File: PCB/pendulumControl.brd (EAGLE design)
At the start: 48 x 41.1 mm, 31 parts, among them IC1 PIC32MX340F512H, IC2 LT1963EST-3.3

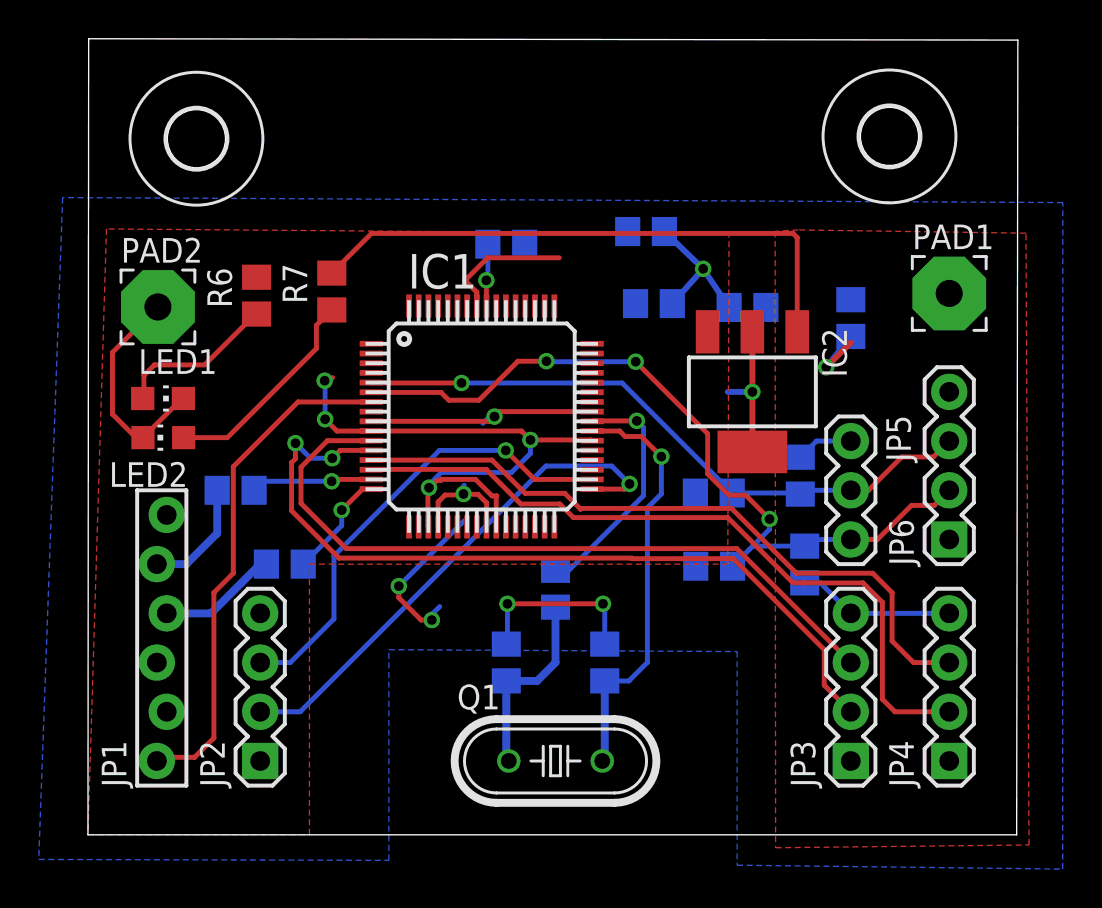
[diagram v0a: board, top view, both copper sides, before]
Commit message: Added MCLR circuit and moved silk screen text around
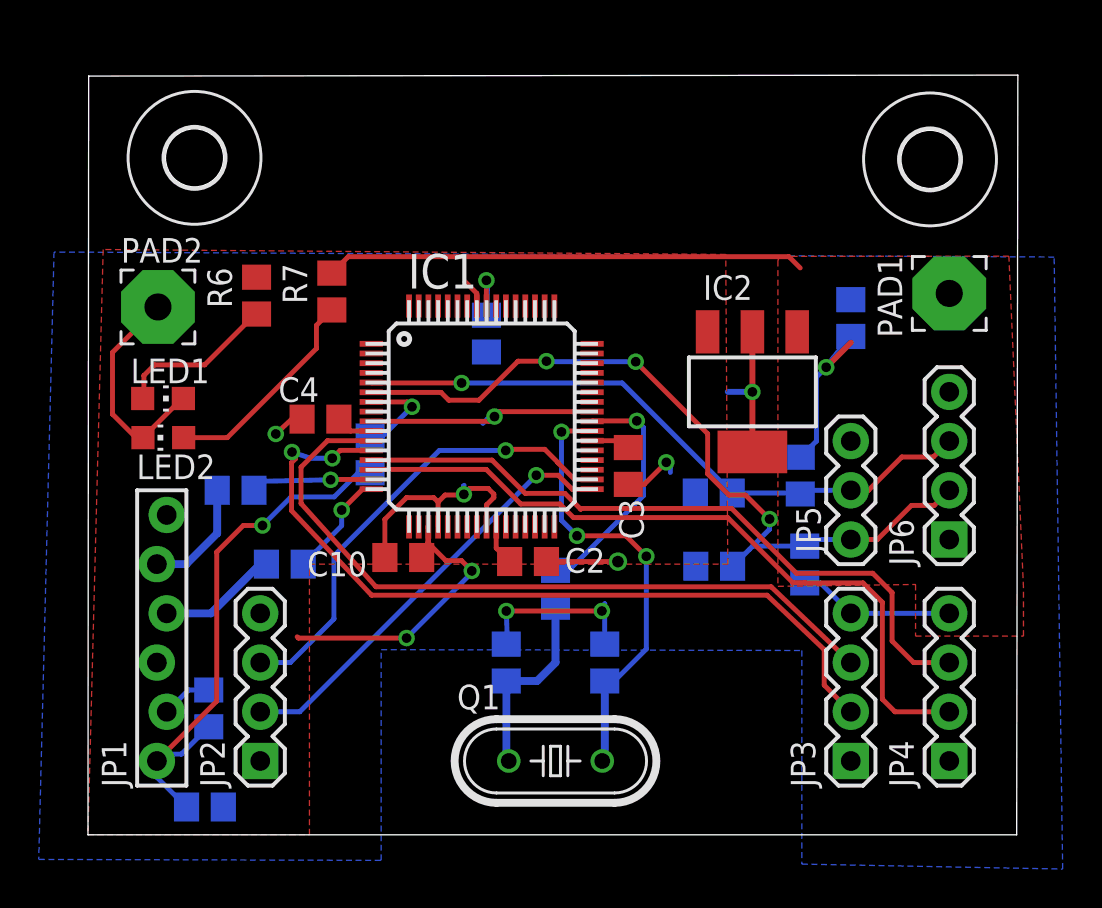
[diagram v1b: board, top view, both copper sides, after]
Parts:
- added C10: 0.1uF, rcl:C0805
- added C11: 100nF, rcl:C0805
- added R8: 10k, resistor:R0805
- added R9: 470, resistor:R0805
- LED1, LED2: value (none) -> GRN
- PAD1: value (none) -> 5V
- PAD2: value (none) -> GND
- Q1: value (none) -> 8MHz
- R4, R5: value (none) -> 3.9k
- R6: value (none) -> 60
- R7: value (none) -> 145
- moved C4 19.4 mm to (12.0, 21.5), flipped to the top, turned to 180 degrees
- moved C2 17.3 mm to (22.7, 14.1), flipped to the top, turned to 0 degrees
- moved C3 8.48 mm to (27.9, 19.0), flipped to the top, turned to 270 degrees
- moved C1 4.73 mm to (20.6, 25.9), turned to 270 degrees
- moved U$2 2.40 mm to (43.5, 34.9)
- moved U$1 0.99 mm to (5.50, 34.9)
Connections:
- new net N$6: C11.1, JP1.1, R8.2, R9.1
- net GND: now also C10.2, C11.2, JP5.1
- net MCLR: now also R9.2; no longer JP1.1
- net VCC3V3: now also C10.1, R8.1
- net VCC5V: no longer JP5.1
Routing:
- net N$6: track 0.00 -> 28.1 mm, vias 0 -> 1
- net MCLR: track 26.4 -> 4.99 mm, vias 0 -> 1
- net VCC3V3: track 45.8 -> 26.3 mm, vias 5 -> 2
- net GND: track 54.4 -> 61.7 mm, vias 7 -> 8
- net TX: track 26.7 -> 22.5 mm
- net VCC5V: track 44.7 -> 41.9 mm
- net OSC1: track 21.9 -> 23.4 mm, vias 1 -> 3
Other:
- board size 48 x 41.1 mm -> 48 x 39.2 mm

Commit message: Finished BOM and moved oscillator closer to the microcontroller
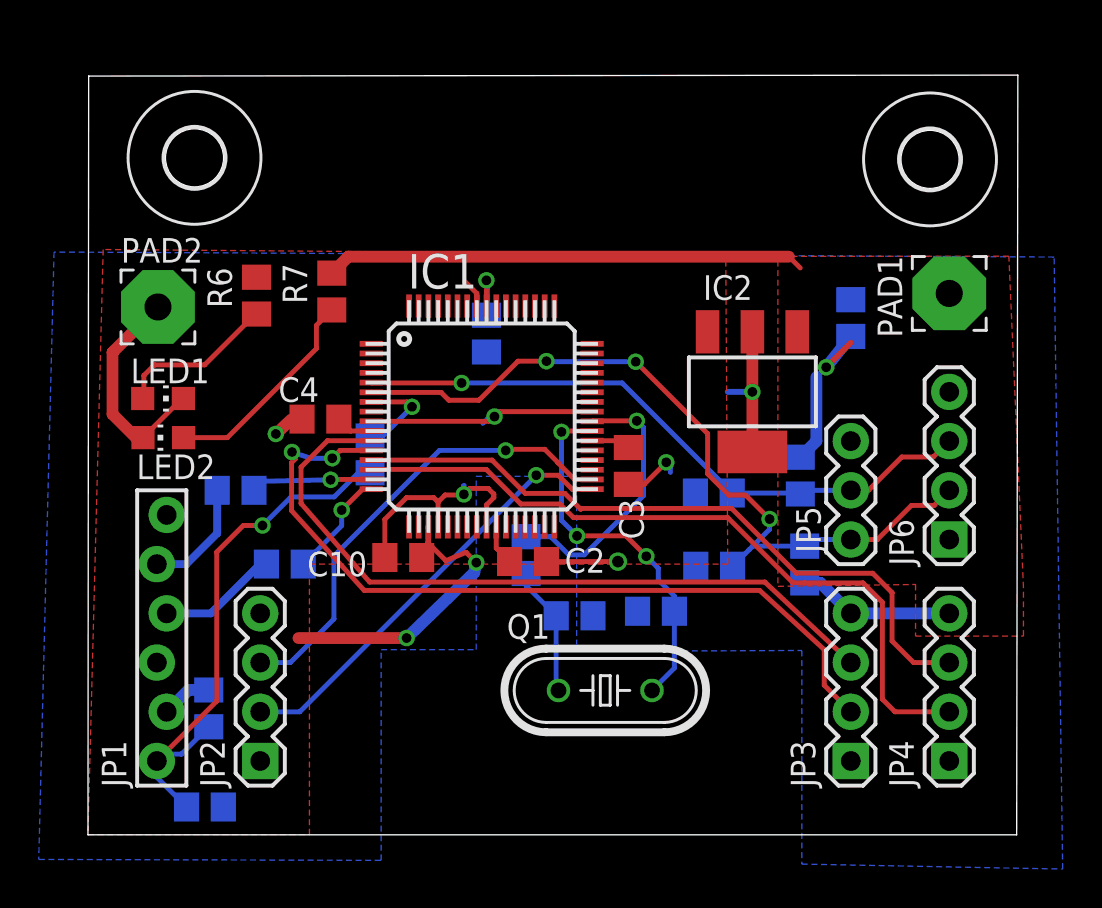
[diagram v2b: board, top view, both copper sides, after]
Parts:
- C9: value 100uF -> 10uF/6.3V
- R1, R2: value 50 -> 47
- moved Q1 4.45 mm to (26.7, 7.45)
- moved C5 4.27 mm to (25.1, 11.3), turned to 180 degrees
- moved C6 3.74 mm to (29.3, 11.5), turned to 0 degrees
- moved R3 2.31 mm to (22.6, 14.4)
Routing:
- net GND: track 61.7 -> 52.6 mm, vias 8 -> 6
- net OSC1: track 23.4 -> 19.3 mm
- net N$3: track 10.1 -> 6.73 mm
- net OSC2: track 12.5 -> 14.0 mm
- net VCC3V3: track 26.3 -> 27.1 mm

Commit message: Getting ready to remove some parts
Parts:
- removed IC2: LT1963EST-3.3, linear-technology:SOT223
- removed JP6: (no value), SparkFun-Connectors:1X04
- C9: value 10uF/6.3V -> 10uF/16V
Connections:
- new net VCC12V: C9.1, PAD1.1, R7.2
- net GND: no longer IC2.2, IC2.4, JP6.1
- net LIM_L: no longer JP6.2
- net LIM_R: no longer JP6.3
- net VCC3V3: no longer IC2.3
- net VCC5V: no longer C9.1, IC2.1, JP6.4, PAD1.1, R7.2
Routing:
- net VCC5V: track 41.9 -> 15.1 mm
- net GND: track 52.6 -> 49.5 mm
- net LIM_R: track 33.3 -> 32.2 mm
- net LIM_L: track 40.7 -> 39.6 mm
- removed copper zone on layer 1, net VCC5V
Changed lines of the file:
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@@
 <element name="C7" library="rcl" package="C0805" value="2.2uF" x="32.29830625" y="17.63914375" rot="MR0"/>
 <element name="C8" library="rcl" package="C0805" value="2.2uF" x="32.318321875" y="13.861490625" rot="MR0"/>
-<element name="C9" library="rcl" package="C0805" value="10uF/6.3V" x="39.37" y="26.67" smashed="yes" rot="MR90">
+<element name="C9" library="rcl" package="C0805" value="10uF/16V" x="39.37" y="26.67" smashed="yes" rot="MR90">
 <attribute name="NAME" x="40.64" y="25.4" size="1.27" layer="26" rot="MR90"/>
 <attribute name="VALUE" x="36.83" y="25.4" size="1.27" layer="28" rot="MR90"/>
@@
 <attribute name="MF" value="" x="20.32" y="21.59" size="1.778" layer="27" display="off"/>
 <attribute name="OC_FARNELL" value="1677915" x="20.32" y="21.59" size="1.778" layer="27" display="off"/>
-</element>
-<element name="IC2" library="linear-technology" package="SOT223" value="LT1963EST-3.3" x="34.29" y="22.86" smashed="yes" rot="R180">
-<attribute name="OC_NEWARK" value="57M7546" x="34.29" y="22.86" size="1.778" layer="27" rot="R180" display="off"/>
-<attribute name="MPN" value="LT1963EST-3.3" x="34.29" y="22.86" size="1.778" layer="27" rot="R180" display="off"/>
-<attribute name="MF" value="" x="34.29" y="22.86" size="1.778" layer="27" rot="R180" display="off"/>
-<attribute name="OC_FARNELL" value="1501032" x="34.29" y="22.86" size="1.778" layer="27" rot="R180" display="off"/>
-<attribute name="NAME" x="31.745071875" y="27.6078125" size="1.27" layer="25"/>
-<attribute name="VALUE" x="29.4132" y="26.162" size="1.27" layer="27" rot="R270"/>
 </element>
 <element name="JP1" library="SparkFun-Connectors" package="1X06_FEMALE_LOCK.010" value="" x="3.81" y="3.81" rot="R90"/>
@@
 <attribute name="VALUE" x="36.195" y="21.59" size="1.27" layer="27" rot="R270"/>
 </element>
-<element name="JP6" library="SparkFun-Connectors" package="1X04" value="" x="44.45" y="15.24" rot="R90"/>
 <element name="LED1" library="led" package="CHIP-LED0805" value="GRN" x="3.874225" y="22.5182125" smashed="yes" rot="R270">
 <attribute name="NAME" x="2.20526875" y="23.3067375" size="1.27" layer="25"/>
@@
 <element name="R7" library="rcl" package="R0805" value="145" x="12.584" y="28.038259375" rot="R90"/>
 <element name="PAD1" library="wirepad" package="3,81/1,4" value="5V" x="44.45" y="27.94" smashed="yes">
-<attribute name="NAME" x="42.0231125" y="25.663696875" size="1.27" layer="25" ratio="10" rot="R90"/>
 <attribute name="VALUE" x="44.45" y="29.14" size="0.0254" layer="27"/>
 </element>
@@
 <signals>
 <signal name="GND">
-<contactref element="IC2" pad="4"/>
 <contactref element="IC1" pad="9"/>
 <contactref element="IC1" pad="20"/>
@@
 <contactref element="C7" pad="2"/>
 <contactref element="C8" pad="2"/>
-<contactref element="JP6" pad="1"/>
 <contactref element="JP3" pad="1"/>
 <contactref element="JP4" pad="1"/>
 <contactref element="LED1" pad="C"/>
 <contactref element="LED2" pad="C"/>
-<contactref element="IC2" pad="2"/>
 <polygon width="0.6096" layer="16">
 <vertex x="-1.750878125" y="30.077321875"/>
@@
 </polygon>
 <contactref element="PAD2" pad="1"/>
-<wire x1="34.29" y1="25.9588" x2="34.29" y2="22.86" width="0.6096" layer="1"/>
 <via x="34.29" y="22.86" extent="1-16" drill="0.5"/>
 <wire x1="34.29" y1="22.86" x2="33.02" y2="22.86" width="0.3048" layer="16"/>
@@
 <wire x1="17.842625" y1="17.402428125" x2="18.07" y2="17.175053125" width="0.254" layer="1"/>
 <contactref element="C11" pad="2"/>
-<wire x1="8.89" y1="3.81" x2="3.556" y2="8.89" width="0" layer="19" extent="1-1"/>
+<wire x1="3.556" y1="8.89" x2="8.89" y2="3.81" width="0" layer="19" extent="1-1"/>
 </signal>
 <signal name="MCLR">
@@
 <contactref element="JP2" pad="4"/>
 <contactref element="R6" pad="2"/>
-<contactref element="IC2" pad="3"/>
 <contactref element="IC1" pad="19"/>
 <polygon width="0.4064" layer="1">
@@
 <wire x1="4.064" y1="6.35" x2="5.189021875" y2="7.475021875" width="0.6096" layer="16"/>
 <wire x1="5.189021875" y1="7.475021875" x2="6.234875" y2="7.475021875" width="0.6096" layer="16"/>
-<wire x1="8.700559375" y1="28.7762" x2="12.950365625" y2="21.452990625" width="0" layer="19" extent="1-1"/>
 </signal>
 <signal name="N$10">
@@
 <contactref element="R4" pad="1"/>
 <contactref element="C7" pad="1"/>
-<contactref element="JP6" pad="3"/>
 <wire x1="39.37" y1="17.78" x2="40.28" y2="17.78" width="0.254" layer="1"/>
 <wire x1="40.28" y1="17.78" x2="42" y2="19.5" width="0.254" layer="1"/>
 <wire x1="42" y1="19.5" x2="43.63" y2="19.5" width="0.254" layer="1"/>
-<wire x1="43.63" y1="19.5" x2="44.45" y2="20.32" width="0.254" layer="1"/>
 <wire x1="36.763821875" y1="17.588409375" x2="36.9554125" y2="17.78" width="0.254" layer="16"/>
 <wire x1="36.9554125" y1="17.78" x2="39.37" y2="17.78" width="0.254" layer="16"/>
@@
 <contactref element="R5" pad="1"/>
 <contactref element="C8" pad="1"/>
-<contactref element="JP6" pad="2"/>
 <wire x1="39.37" y1="15.24" x2="40.74" y2="15.24" width="0.254" layer="1"/>
 <wire x1="40.74" y1="15.24" x2="42.5" y2="17" width="0.254" layer="1"/>
 <wire x1="42.5" y1="17" x2="43.67" y2="17" width="0.254" layer="1"/>
-<wire x1="43.67" y1="17" x2="44.45" y2="17.78" width="0.254" layer="1"/>
 <wire x1="33.268321875" y1="13.861490625" x2="34.130028125" y2="14.723196875" width="0.254" layer="16"/>
 <wire x1="34.130028125" y1="14.723196875" x2="34.306840625" y2="14.900009375" width="0.254" layer="16"/>
@@
 <contactref element="R4" pad="2"/>
 <contactref element="R5" pad="2"/>
-<contactref element="C9" pad="1"/>
-<contactref element="JP6" pad="4"/>
 <contactref element="JP3" pad="4"/>
 <contactref element="JP4" pad="4"/>
-<contactref element="R7" pad="2"/>
-<contactref element="IC2" pad="1"/>
-<contactref element="PAD1" pad="1"/>
-<polygon width="0.4064" layer="1">
-<vertex x="35.695459375" y="29.854"/>
-<vertex x="35.606740625" y="29.638153125"/>
-<vertex x="35.60725625" y="12.823328125"/>
-<vertex x="42.6398625" y="12.91930625"/>
-<vertex x="42.71120625" y="12.91930625"/>
-<vertex x="42.71120625" y="10.25455"/>
-<vertex x="48.280928125" y="10.25455"/>
-<vertex x="48.280928125" y="12.752709375"/>
-<vertex x="47.526678125" y="29.863284375"/>
-</polygon>
-<wire x1="39.37" y1="25.72" x2="38.1" y2="24.13" width="0.6096" layer="16"/>
 <via x="38.1" y="24.13" extent="1-16" drill="0.5"/>
 <wire x1="38.1" y1="24.13" x2="39.37" y2="25.4" width="0.3048" layer="1"/>
@@
 <wire x1="37.5954125" y1="20.32" x2="37.5954125" y2="23.6254125" width="0.6096" layer="16"/>
 <wire x1="37.5954125" y1="23.6254125" x2="38.1" y2="24.13" width="0.254" layer="16"/>
-<wire x1="12.584" y1="28.988259375" x2="13.433625" y2="29.837884375" width="0.6096" layer="1"/>
-<wire x1="13.433625" y1="29.837884375" x2="36.178353125" y2="29.837884375" width="0.6096" layer="1"/>
-<wire x1="36.178353125" y1="29.837884375" x2="36.7592875" y2="29.25695" width="0.254" layer="1"/>
+<wire x1="36.989853125" y1="13.000009375" x2="36.763821875" y2="19.488409375" width="0" layer="19" extent="16-16"/>
 </signal>
 <signal name="N$4">
@@
 <wire x1="3.909575" y1="4.163575" x2="3.556" y2="3.81" width="0.254" layer="16"/>
 </signal>
+<signal name="VCC12V">
+<contactref element="PAD1" pad="1"/>
+<contactref element="C9" pad="1"/>
+<contactref element="R7" pad="2"/>
+<wire x1="39.37" y1="25.72" x2="44.45" y2="27.94" width="0" layer="19" extent="16-16"/>
+<wire x1="12.584" y1="28.988259375" x2="39.37" y2="25.72" width="0" layer="19" extent="1-16"/>
+</signal>
 </signals>

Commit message: Updated the PCB
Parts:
- removed C7, C8: 2.2uF, rcl:C0805
- removed JP3, JP4: (no value), SparkFun-Connectors:1X04
- removed JP5: (no value), SparkFun-Connectors:1X03
- removed LED1: GRN, led:CHIP-LED0805
- removed R4, R5: 3.9k, rcl:R0805
- added 3.3V: GRN, led:CHIP-LED0805
- added ARM, MOTOR: (no value), SparkFun-Connectors:1X03
- added FAN: (no value), SparkFun-Connectors:MOLEX-1X3
- added IC2: (no value), v-reg:78MXXS
- added LIMITS: (no value), SparkFun-Connectors:1X02
- R7: value 145 -> (none)
- moved C3 0.35 mm to (27.6, 18.9)
- renumbered JP1 to PROGRAMMING, JP2 to USB-UART, LED2 to 12V, PAD1 to 24V, PAD2 to GND
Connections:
- removed net VCC5V: JP3.4, JP4.4, R4.2, R5.2
- new net VCC24V: 24V.1, IC2.IN
- net ARM_CHA: now also ARM.3; no longer JP3.3
- net ARM_CHB: now also ARM.2; no longer JP3.2
- net GND: now also 3.3V.C, ARM.1, FAN.1, IC2.GND, MOTOR.1; no longer C7.2, C8.2, JP3.1, JP4.1, JP5.1, LED1.C
- net LIM_L: now also LIMITS.2; no longer C8.1, JP5.3, R5.1
- net LIM_R: now also LIMITS.1; no longer C7.1, JP5.2, R4.1
- net M_CHA: now also MOTOR.3; no longer JP4.3
- net M_CHB: now also MOTOR.2; no longer JP4.2
- net N$4: now also 3.3V.A; no longer LED1.A
- net VCC12V: now also FAN.2, IC2.OUT; no longer 24V.1
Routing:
- net VCC12V: track 0.00 -> 45.8 mm
- net GND: track 49.5 -> 71.6 mm, vias 6 -> 9
- net VCC5V: track 15.1 -> 0.00 mm, vias 1 -> 0
- net VCC3V3: track 27.1 -> 40.4 mm
- net LIM_R: track 32.2 -> 38.9 mm
- net OSC2: track 14.0 -> 19.8 mm
- net VCC24V: track 0.00 -> 5.32 mm
- net LIM_L: track 39.6 -> 35.6 mm, vias 3 -> 1
- net ARM_CHB: track 41.7 -> 38.3 mm
- net RX: track 24.2 -> 21.1 mm
- net N$4: track 8.34 -> 5.92 mm
- net MCLR: track 4.99 -> 7.39 mm
- net OSC1: track 19.3 -> 18.3 mm, vias 3 -> 1
- net M_CHB: track 37.9 -> 37.0 mm, vias 0 -> 1
- net N$5: track 11.1 -> 10.4 mm
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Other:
- board text added: "1"
- board text added: "CH A"
- board text added: "CH B"
- board text added: "FAN"
- board text added: "GND"
- board text added: "L"
- board text added: "R"

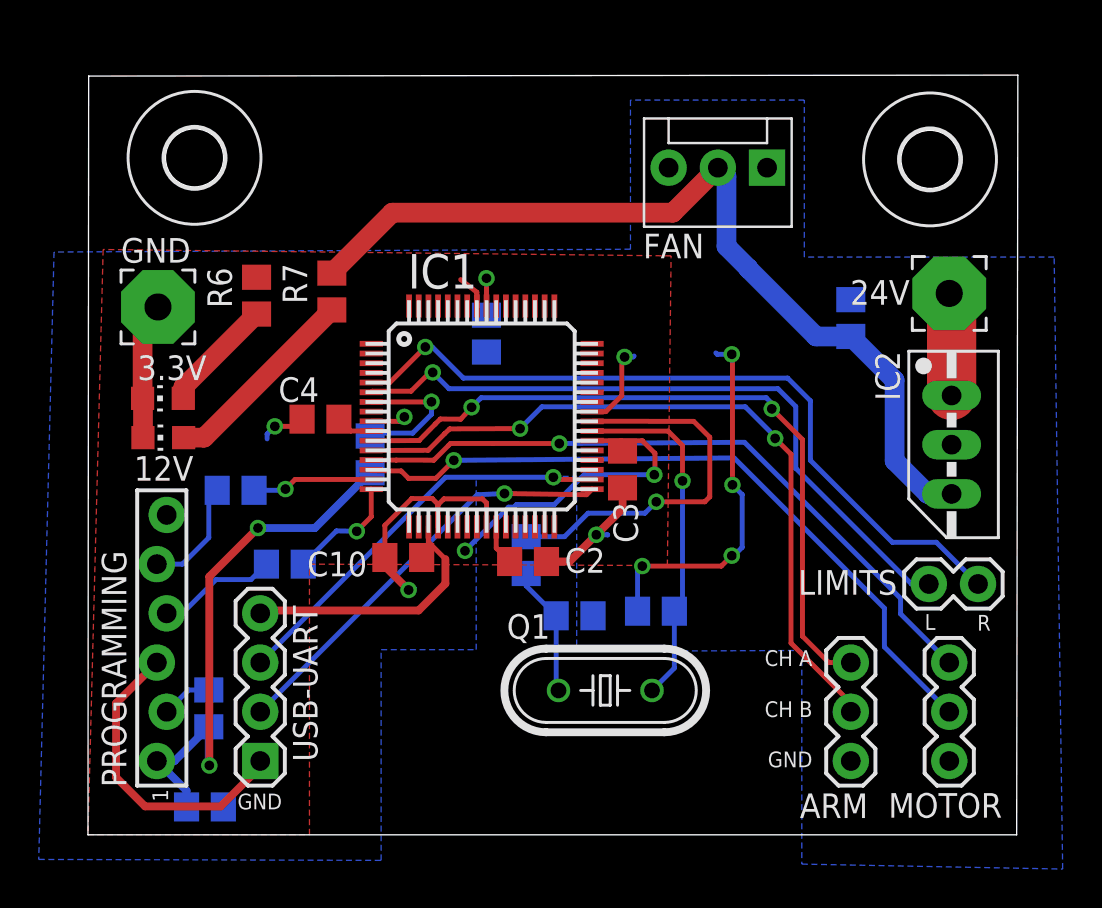
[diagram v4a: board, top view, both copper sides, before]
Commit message: Added smoothing caps to the limit switches.
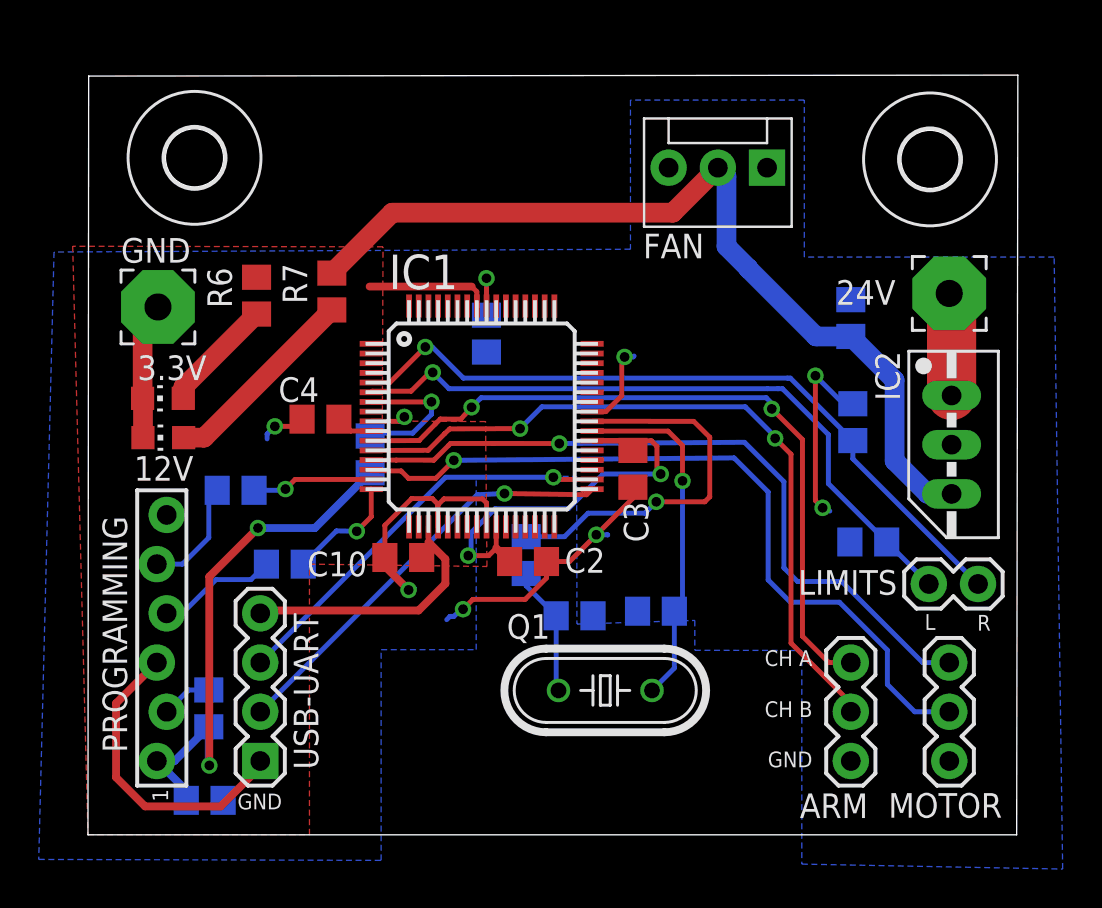
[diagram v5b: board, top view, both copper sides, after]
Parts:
- added C7, C8: 0.022uF, rcl:C0805
- moved C3 0.54 mm to (28.1, 18.9)
- moved C11 0.34 mm to (6.02, 1.78)
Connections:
- net GND: now also C7.2, C8.2
- net LIM_L: now also C8.1
- net LIM_R: now also C7.1
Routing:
- net VCC3V3: track 40.4 -> 49.4 mm
- net M_CHB: track 37.0 -> 39.5 mm
- net M_CHA: track 35.4 -> 37.5 mm
- net GND: track 71.6 -> 69.7 mm, vias 9 -> 8
- net LIM_R: track 38.9 -> 37.7 mm
